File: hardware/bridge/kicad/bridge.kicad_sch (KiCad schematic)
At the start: 0 parts

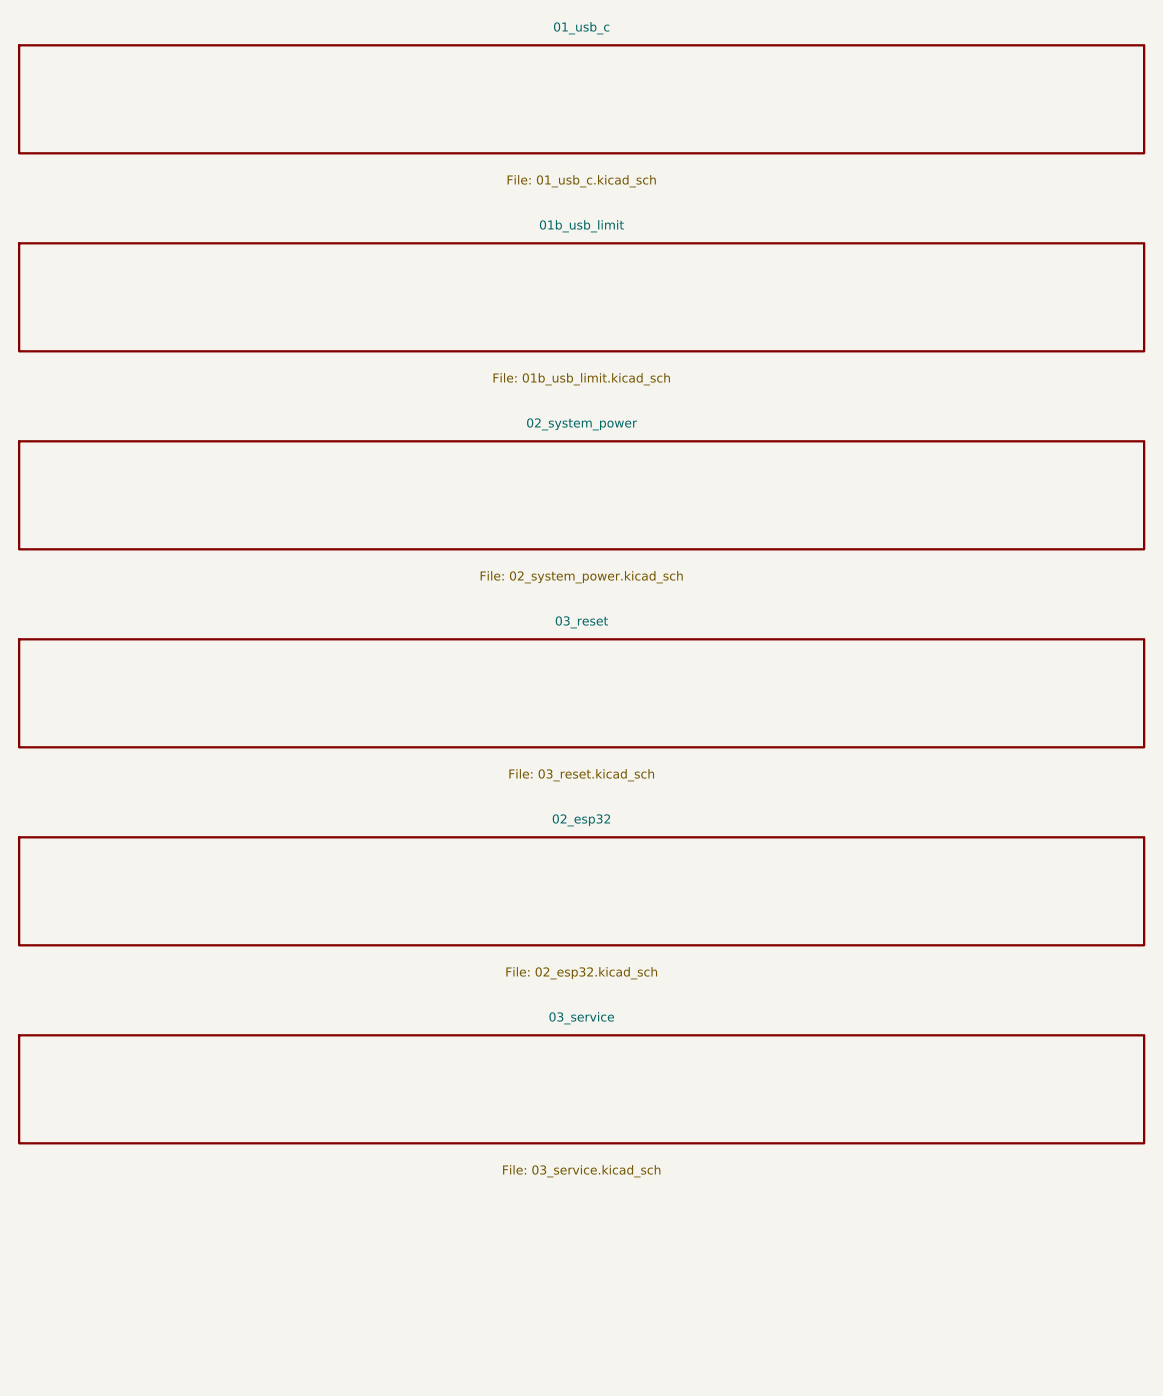
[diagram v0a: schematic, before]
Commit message: fix: close hardware rail-fault paths and sensor contract gaps
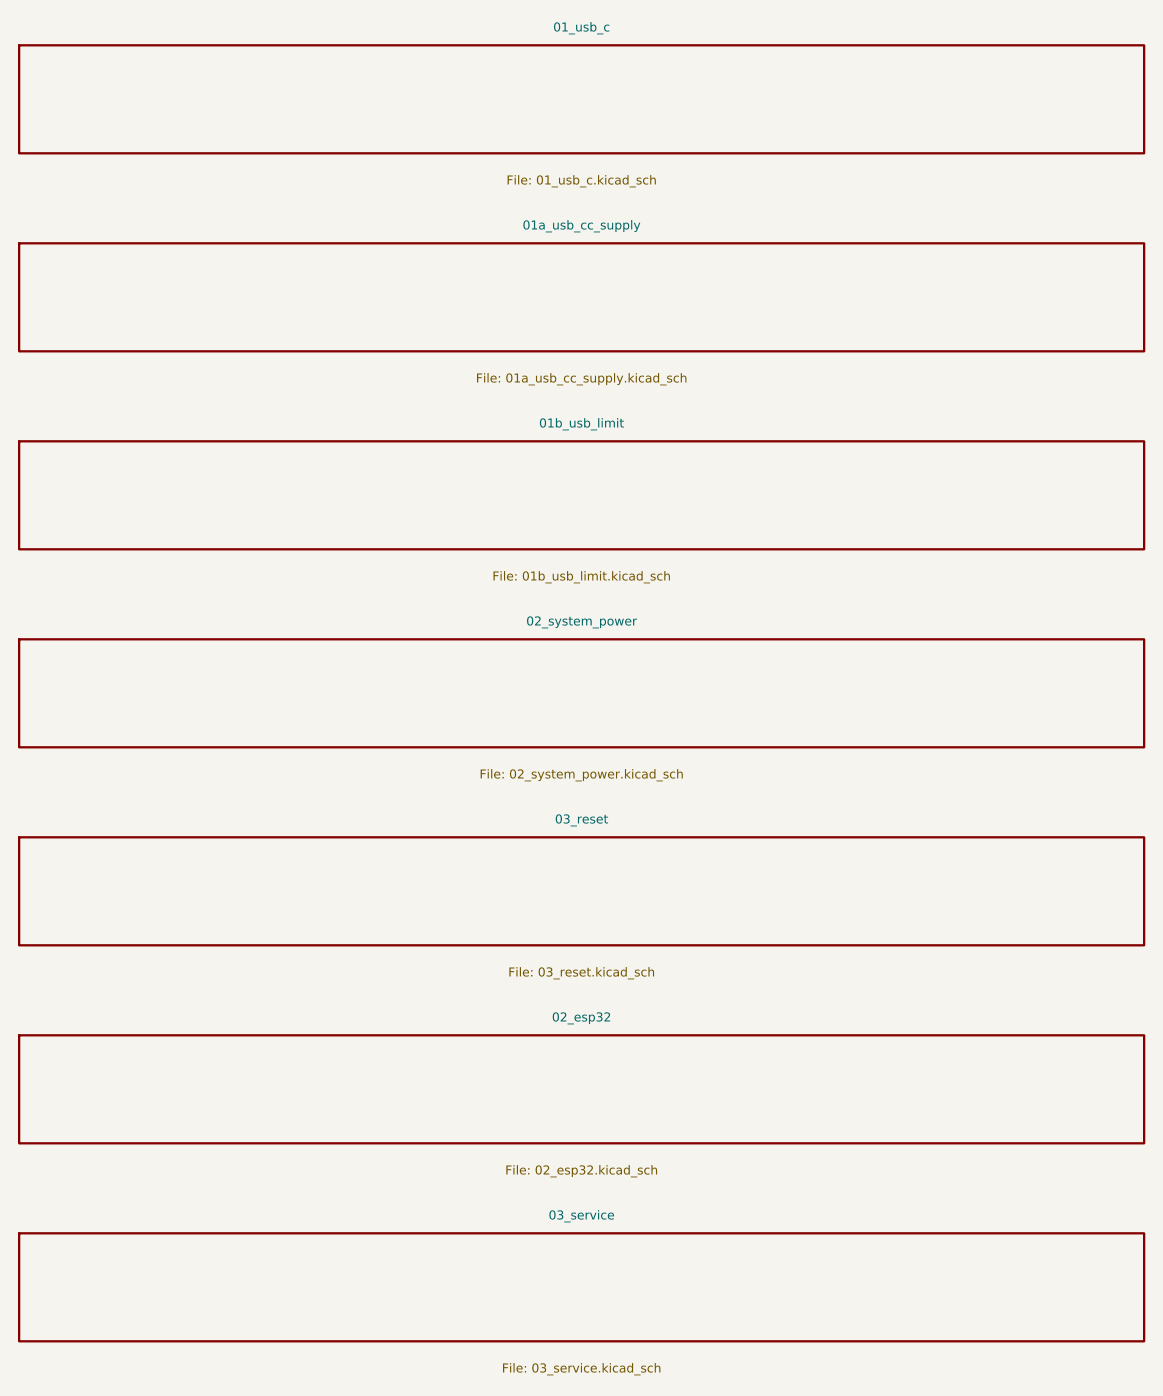
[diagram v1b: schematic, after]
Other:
- added sheet 01a_usb_cc_supply (01a_usb_cc_supply.kicad_sch)
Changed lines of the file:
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@@
 (kicad_sch (version 20250114) (generator "eeschema") (generator_version "10.0") (paper "A3") (title_block (title "CANView / bridge") (date "2026-09-05") (rev "R1 REVIEW") (company "digitie/canview") (comment 1 "SCHEMATIC REVIEW ONLY - PCB/HIL release gates remain open"))
 (sheet (at 17 30) (size 125 12) (stroke (width 0.254) (type default)) (fill (color 0 0 0 0)) (property "Sheetname" "01_usb_c" (at 79.5000 28.0000 0)  (effects (font (size 1.0 1.0)) )) (property "Sheetfile" "01_usb_c.kicad_sch" (at 79.5000 45.0000 0)  (effects (font (size 1.0 1.0)) )) (instances (project "bridge" (path "/695535dc-1835-5369-a035-dbad415d33c6" (page "2")))))
-(sheet (at 17 52) (size 125 12) (stroke (width 0.254) (type default)) (fill (color 0 0 0 0)) (property "Sheetname" "01b_usb_limit" (at 79.5000 50.0000 0)  (effects (font (size 1.0 1.0)) )) (property "Sheetfile" "01b_usb_limit.kicad_sch" (at 79.5000 67.0000 0)  (effects (font (size 1.0 1.0)) )) (instances (project "bridge" (path "/695535dc-1835-5369-a035-dbad415d33c6" (page "3")))))
-(sheet (at 17 74) (size 125 12) (stroke (width 0.254) (type default)) (fill (color 0 0 0 0)) (property "Sheetname" "02_system_power" (at 79.5000 72.0000 0)  (effects (font (size 1.0 1.0)) )) (property "Sheetfile" "02_system_power.kicad_sch" (at 79.5000 89.0000 0)  (effects (font (size 1.0 1.0)) )) (instances (project "bridge" (path "/695535dc-1835-5369-a035-dbad415d33c6" (page "4")))))
-(sheet (at 17 96) (size 125 12) (stroke (width 0.254) (type default)) (fill (color 0 0 0 0)) (property "Sheetname" "03_reset" (at 79.5000 94.0000 0)  (effects (font (size 1.0 1.0)) )) (property "Sheetfile" "03_reset.kicad_sch" (at 79.5000 111.0000 0)  (effects (font (size 1.0 1.0)) )) (instances (project "bridge" (path "/695535dc-1835-5369-a035-dbad415d33c6" (page "5")))))
-(sheet (at 17 118) (size 125 12) (stroke (width 0.254) (type default)) (fill (color 0 0 0 0)) (property "Sheetname" "02_esp32" (at 79.5000 116.0000 0)  (effects (font (size 1.0 1.0)) )) (property "Sheetfile" "02_esp32.kicad_sch" (at 79.5000 133.0000 0)  (effects (font (size 1.0 1.0)) )) (instances (project "bridge" (path "/695535dc-1835-5369-a035-dbad415d33c6" (page "6")))))
-(sheet (at 17 140) (size 125 12) (stroke (width 0.254) (type default)) (fill (color 0 0 0 0)) (property "Sheetname" "03_service" (at 79.5000 138.0000 0)  (effects (font (size 1.0 1.0)) )) (property "Sheetfile" "03_service.kicad_sch" (at 79.5000 155.0000 0)  (effects (font (size 1.0 1.0)) )) (instances (project "bridge" (path "/695535dc-1835-5369-a035-dbad415d33c6" (page "7")))))
+(sheet (at 17 52) (size 125 12) (stroke (width 0.254) (type default)) (fill (color 0 0 0 0)) (property "Sheetname" "01a_usb_cc_supply" (at 79.5000 50.0000 0)  (effects (font (size 1.0 1.0)) )) (property "Sheetfile" "01a_usb_cc_supply.kicad_sch" (at 79.5000 67.0000 0)  (effects (font (size 1.0 1.0)) )) (instances (project "bridge" (path "/695535dc-1835-5369-a035-dbad415d33c6" (page "3")))))
+(sheet (at 17 74) (size 125 12) (stroke (width 0.254) (type default)) (fill (color 0 0 0 0)) (property "Sheetname" "01b_usb_limit" (at 79.5000 72.0000 0)  (effects (font (size 1.0 1.0)) )) (property "Sheetfile" "01b_usb_limit.kicad_sch" (at 79.5000 89.0000 0)  (effects (font (size 1.0 1.0)) )) (instances (project "bridge" (path "/695535dc-1835-5369-a035-dbad415d33c6" (page "4")))))
+(sheet (at 17 96) (size 125 12) (stroke (width 0.254) (type default)) (fill (color 0 0 0 0)) (property "Sheetname" "02_system_power" (at 79.5000 94.0000 0)  (effects (font (size 1.0 1.0)) )) (property "Sheetfile" "02_system_power.kicad_sch" (at 79.5000 111.0000 0)  (effects (font (size 1.0 1.0)) )) (instances (project "bridge" (path "/695535dc-1835-5369-a035-dbad415d33c6" (page "5")))))
+(sheet (at 17 118) (size 125 12) (stroke (width 0.254) (type default)) (fill (color 0 0 0 0)) (property "Sheetname" "03_reset" (at 79.5000 116.0000 0)  (effects (font (size 1.0 1.0)) )) (property "Sheetfile" "03_reset.kicad_sch" (at 79.5000 133.0000 0)  (effects (font (size 1.0 1.0)) )) (instances (project "bridge" (path "/695535dc-1835-5369-a035-dbad415d33c6" (page "6")))))
+(sheet (at 17 140) (size 125 12) (stroke (width 0.254) (type default)) (fill (color 0 0 0 0)) (property "Sheetname" "02_esp32" (at 79.5000 138.0000 0)  (effects (font (size 1.0 1.0)) )) (property "Sheetfile" "02_esp32.kicad_sch" (at 79.5000 155.0000 0)  (effects (font (size 1.0 1.0)) )) (instances (project "bridge" (path "/695535dc-1835-5369-a035-dbad415d33c6" (page "7")))))
+(sheet (at 17 162) (size 125 12) (stroke (width 0.254) (type default)) (fill (color 0 0 0 0)) (property "Sheetname" "03_service" (at 79.5000 160.0000 0)  (effects (font (size 1.0 1.0)) )) (property "Sheetfile" "03_service.kicad_sch" (at 79.5000 177.0000 0)  (effects (font (size 1.0 1.0)) )) (instances (project "bridge" (path "/695535dc-1835-5369-a035-dbad415d33c6" (page "8")))))
 (sheet_instances (path "/" (page "1")))
 )
